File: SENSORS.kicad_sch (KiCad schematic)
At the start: 20 parts, among them U14 ICM-42688-P, U15 ICM-42688-P, U16 DPS368XTSA1, U17 IST8310

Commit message: Remove unused file
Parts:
- removed C47, C50: 100n, Capacitor_SMD:C_0402_1005Metric, symbol Device:C_Small
- removed R25, R26: 4.7K, Resistor_SMD:R_0402_1005Metric, symbol Device:R_Small
- removed R29: 100K, Resistor_SMD:R_0402_1005Metric, symbol Device:R_Small
- removed U17: IST8310, EasyEDA:LGA-16_L3.0-W3.0-P0.50-BL_SQ, symbol EasyEDA:HMC5883L-TR
- added C68: 100n, Capacitor_SMD:C_0402_1005Metric, symbol Device:C_Small
- added J10, J15: Conn_01x04, symbol Connector_Generic:Conn_01x04
- added R52, R53, R54, R55: 4.7K, Resistor_SMD:R_0402_1005Metric, symbol Device:R_Small
- added U2: BMP581, QFN10_BMP581_BOS, symbol BMP581:BMP581
- C51: value 4.7u -> 100n; LCSC C23733 -> C1525; LCSC Part C23733 -> C1525; MPN CL05A475MP5NRNC -> GRM022R60J104KE15D; Manufacturer Samsung Electro-Mechanics -> Murata Electronics
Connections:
- net +3V3_MCU: now also C49.1, U16.2 (CSB), U16.6 (VDDIO), C68.1, R52.1, R53.1, R54.1, R55.1, U2.1 (VDDIO), U2.6 (CSB)
- net +3V3_SENS: now also C51.1, U2.10 (VDD); no longer C49.1, U16.2 (CSB), U16.6 (VDDIO)
- net GND: now also C68.2, J10.2 (Pin_2), J15.2 (Pin_2), U2.3 (VSS), U2.5 (SDO), U2.8 (VSS), U2.9 (VSS)
- net I2C2.SCL: now also J15.4 (Pin_4), R54.2
- net I2C2.SDA: now also J15.3 (Pin_3), R55.2
- new net +5V_SYS: J10.1 (Pin_1), J15.1 (Pin_1)
- new net I2C1.SCL: J10.4 (Pin_4), R52.2, U2.2 (SCK)
- new net I2C1.SDA: J10.3 (Pin_3), R53.2, U2.4 (SDI)
- no-connect marks 9 -> 1
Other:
- note added: "I2C_1"
- note added: "I2C_2"
- note added: "shared with DPS368 sur I2C2 BMP581 sur I2C1"
- moved on the sheet: C48, U16

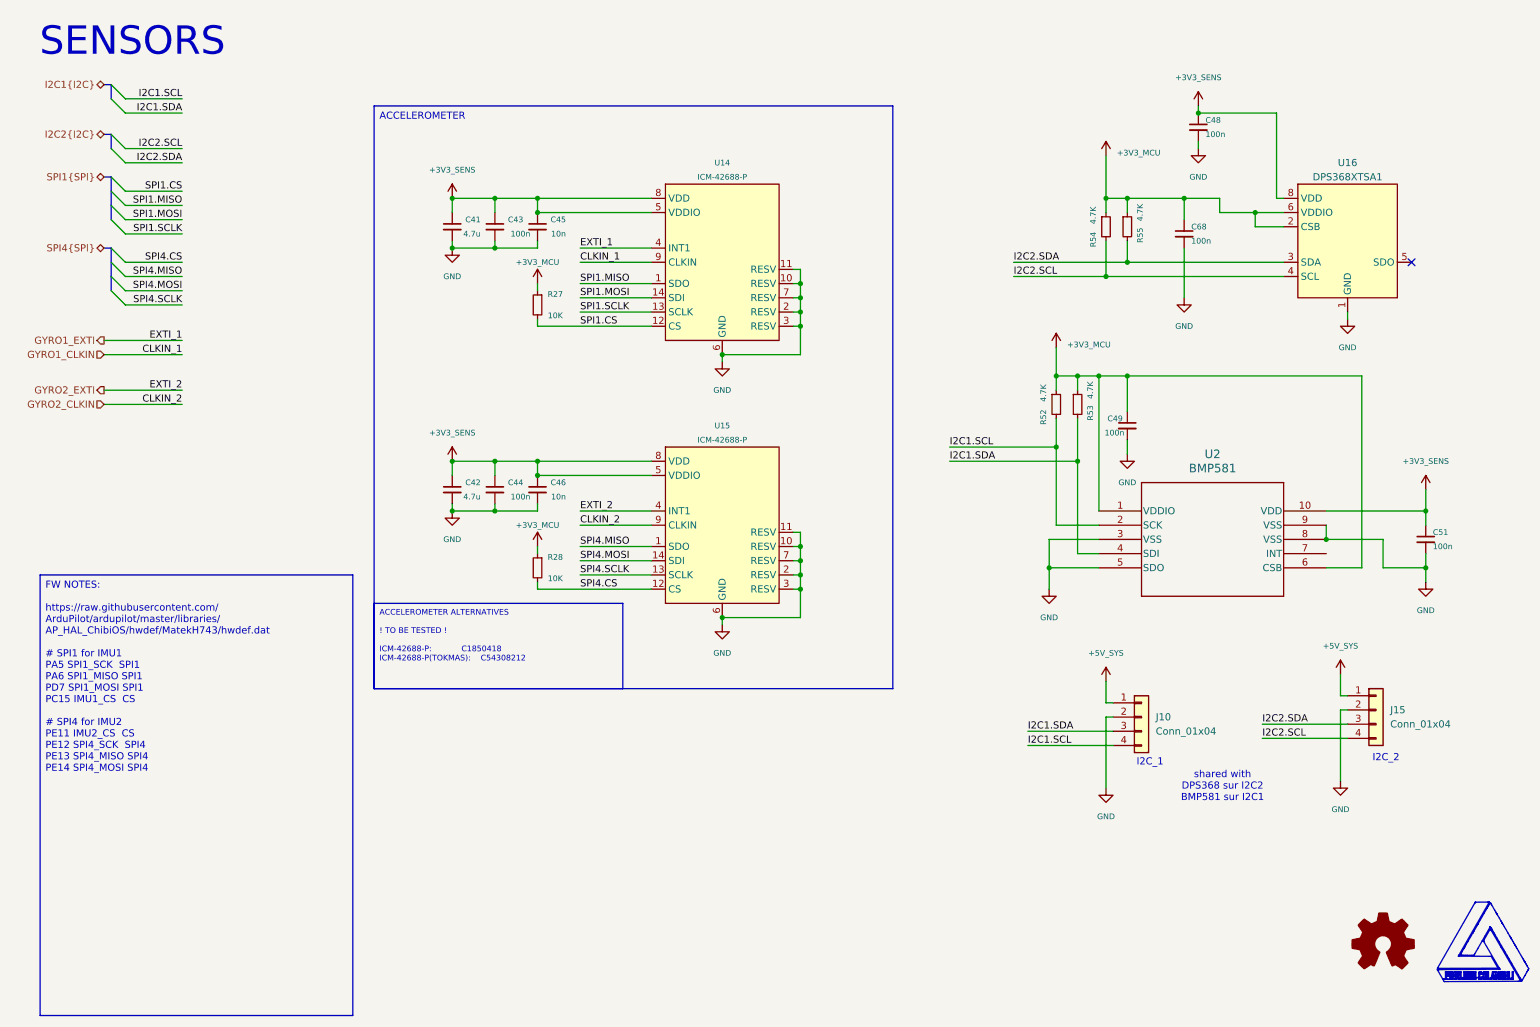
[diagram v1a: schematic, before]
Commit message: rework and work on IMUs
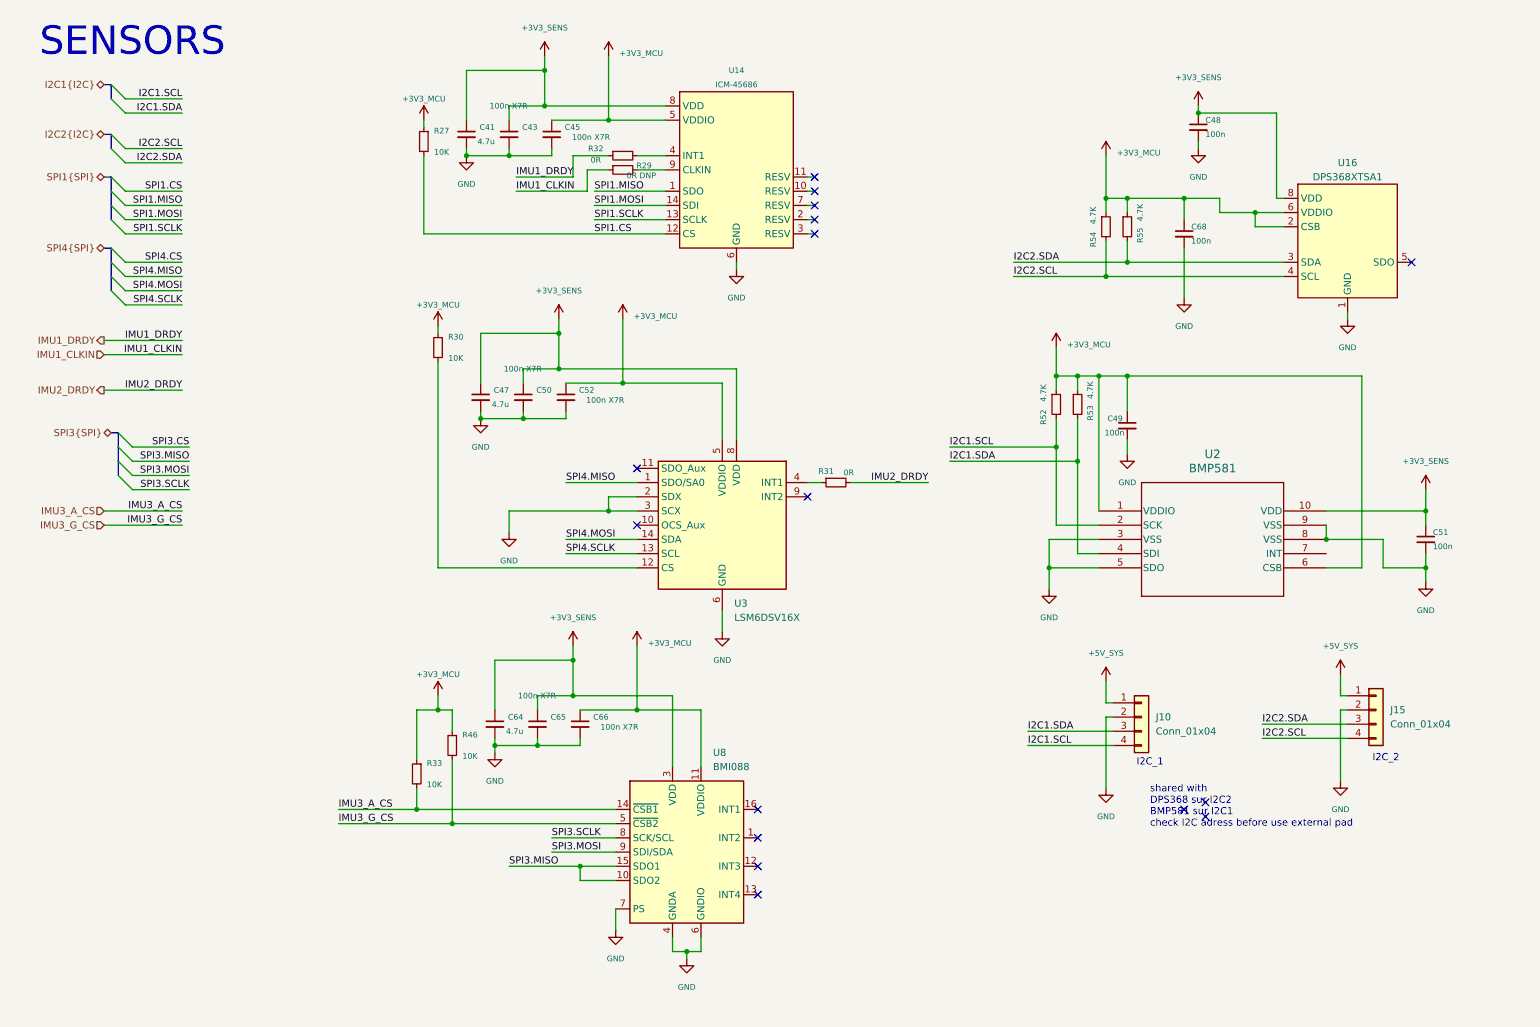
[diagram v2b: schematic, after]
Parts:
- removed C42: 4.7u, Capacitor_SMD:C_0402_1005Metric, symbol Device:C_Small
- removed C44: 100n, Capacitor_SMD:C_0402_1005Metric, symbol Device:C_Small
- removed C46: 10n, Capacitor_SMD:C_0402_1005Metric, symbol Device:C_Small
- removed R28: 10K, Resistor_SMD:R_0402_1005Metric, symbol Device:R_Small
- removed U15: ICM-42688-P, EasyEDA:LGA-14_L3.0-W2.5-P0.50-TL, symbol EasyEDA:ICM-42688-P
- added C47, C64: 4.7u, Capacitor_SMD:C_0402_1005Metric, symbol Device:C_Small
- added C50, C52, C65, C66: 100n X7R, Capacitor_SMD:C_0402_1005Metric, symbol Device:C_Small
- added R29: 0R DNP, Resistor_SMD:R_0402_1005Metric, symbol Device:R_Small
- added R30, R33, R46: 10K, Resistor_SMD:R_0402_1005Metric, symbol Device:R_Small
- added R31, R32: 0R, Resistor_SMD:R_0402_1005Metric, symbol Device:R_Small
- added U3: LSM6DSV16X, Package_LGA:LGA-14_3x2.5mm_P0.5mm_LayoutBorder3x4y, symbol Sensor_Motion:LSM6DSM
- added U8: BMI088, Package_LGA:Bosch_LGA-16_4.5x3mm_P0.5mm_LayoutBorder7x1y_ClockwisePinNumbering, symbol Sensor_Motion:BMI088
- C43: value 100n -> 100n X7R
- C45: value 10n -> 100n X7R
- U14: value ICM-42688-P -> ICM-45686
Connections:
- net +3V3_MCU: now also C45.1, U14.5 (VDDIO), C52.1, C66.1, R30.1, R33.1, R46.1, U3.5 (VDDIO), U8.11 (VDDIO)
- net +3V3_SENS: now also C47.1, C50.1, C64.1, C65.1, U3.8 (VDD), U8.3 (VDD); no longer C45.1, U14.5 (VDDIO)
- net GND: now also C47.2, C50.2, C52.2, C64.2, C65.2, C66.2, U3.2 (SDX), U3.3 (SCX), U3.6 (GND), U3.7 (GND), U8.2 (GNDA), U8.4 (GNDA), U8.6 (GNDIO), U8.7 (PS); no longer U14.10 (RESV), U14.11 (RESV), U14.2 (RESV), U14.3 (RESV), U14.7 (RESV)
- net SPI4.MISO: now also U3.1 (SDO/SA0)
- net SPI4.MOSI: now also U3.14 (SDA)
- net SPI4.SCLK: now also U3.13 (SCL)
- net GYRO1_CLKIN: no longer names the net of U14.9 (CLKIN)
- net GYRO1_CLKIN: now also R29.2
- net GYRO1_EXTI: no longer names the net of U14.4 (INT1)
- net GYRO1_EXTI: now also R32.2
- new net: R30.2, U3.12 (CS)
- new net: R31.1, U3.4 (INT1)
- new net IMU1_CLKIN: R29.1
- new net IMU1_DRDY: R32.1
- new net IMU2_DRDY: R31.2
- new net IMU3_A_CS: R33.2, U8.14 (~{CSB1})
- new net IMU3_G_CS: R46.2, U8.5 (~{CSB2})
- new net SPI3.MISO: U8.10 (SDO2), U8.15 (SDO1)
- new net SPI3.MOSI: U8.9 (SDI/SDA)
- new net SPI3.SCLK: U8.8 (SCK/SCL)
- no-connect marks 1 -> 16
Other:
- note added: "shared with DPS368 sur I2C2 BMP581 sur I2C1 check I2C adress before use external pad"
- note removed: "shared with DPS368 sur I2C2 BMP581 sur I2C1"
- moved on the sheet: C41, C43, C45, R27, U14

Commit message: update name
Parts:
- removed R27, R30, R33, R46: 10K, Resistor_SMD:R_0402_1005Metric, symbol Device:R_Small
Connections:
- net SPI4.CS: now also U3.12 (CS)
- no-connect marks 16 -> 13
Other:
- note removed: "SENSORS"
- company: Pierluigi Colangeli, PhD -> (none)
- title: LEVIA H7 -> (none)

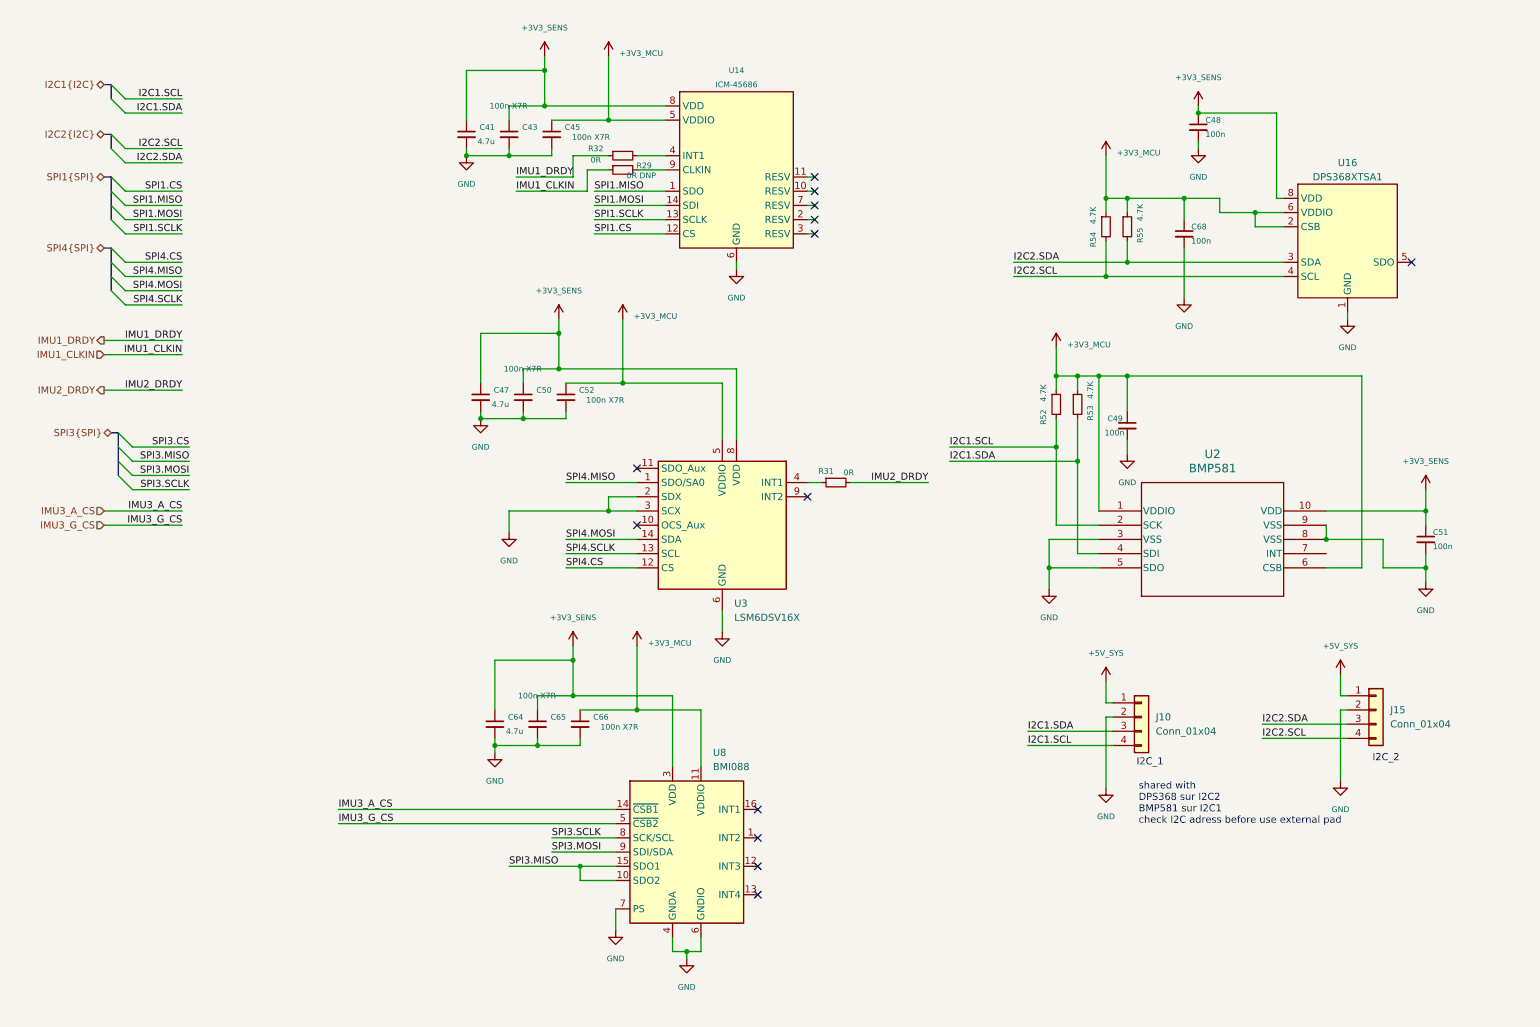
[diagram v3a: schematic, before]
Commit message: upsadte SPI4 set to Baro
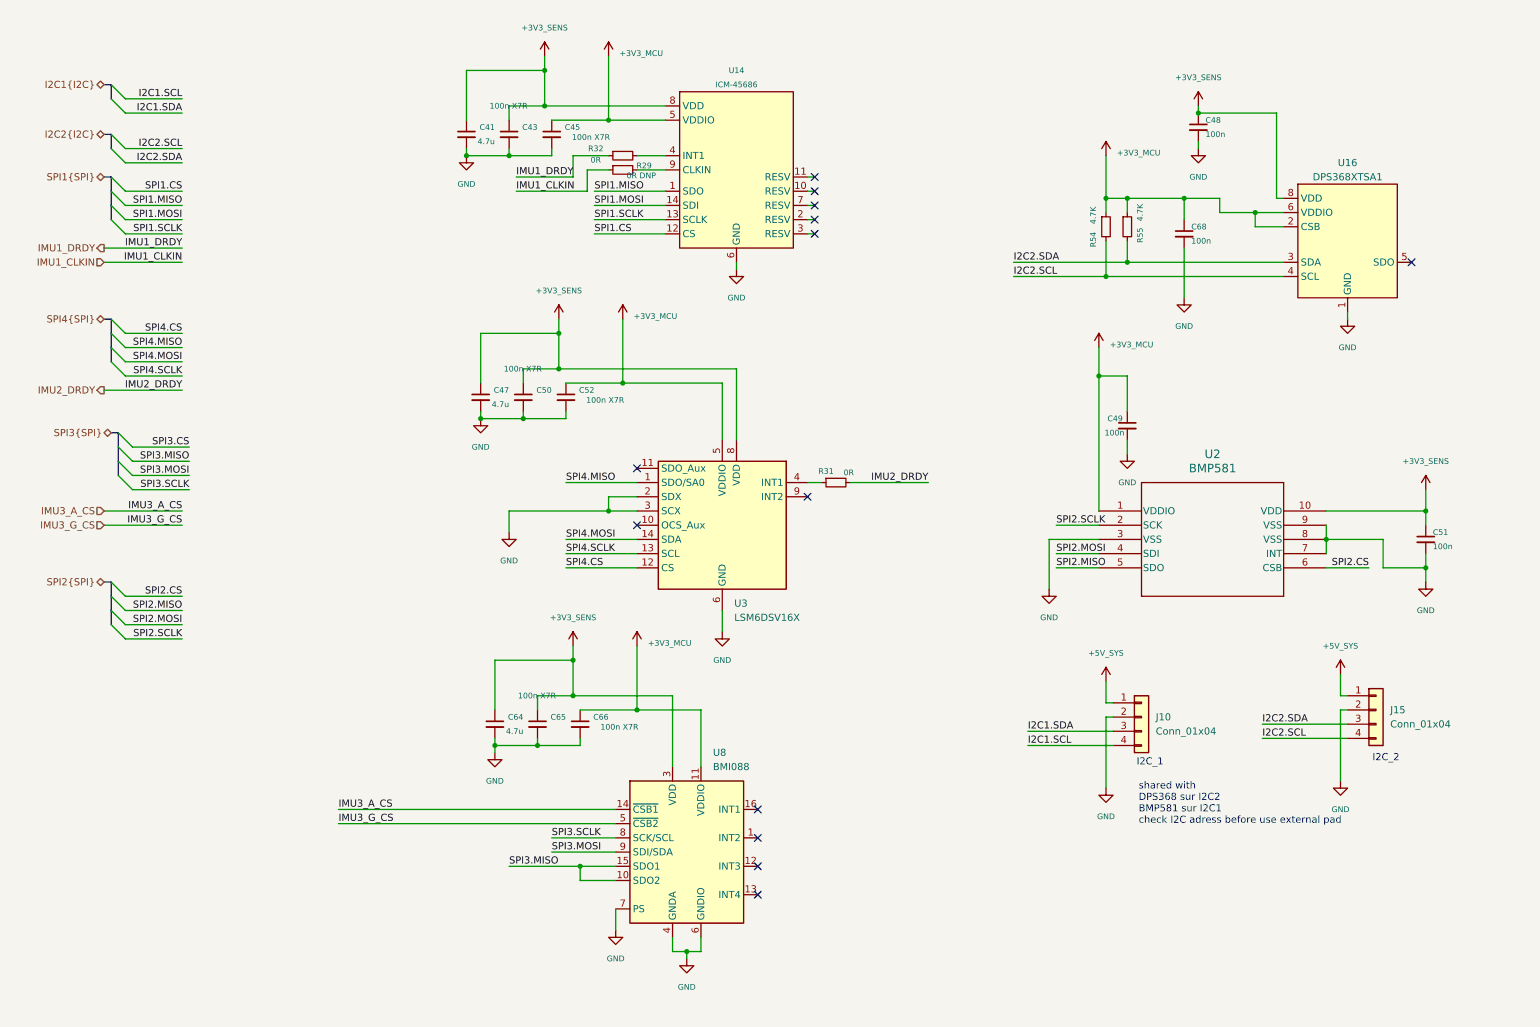
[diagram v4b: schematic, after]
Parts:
- removed R52, R53: 4.7K, Resistor_SMD:R_0402_1005Metric, symbol Device:R_Small
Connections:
- net +3V3_MCU: no longer U2.6 (CSB)
- net GND: now also U2.7 (INT); no longer U2.5 (SDO)
- net I2C1.SCL: no longer U2.2 (SCK)
- net I2C1.SDA: no longer U2.4 (SDI)
- new net SPI2.CS: U2.6 (CSB)
- new net SPI2.MISO: U2.5 (SDO)
- new net SPI2.MOSI: U2.4 (SDI)
- new net SPI2.SCLK: U2.2 (SCK)
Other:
- title: (none) -> H743_ARDUPILOT

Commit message: update 1
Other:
- note removed: "shared with DPS368 sur I2C2 BMP581 sur I2C1 check I2C adress before use external pad"
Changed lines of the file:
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@@
-		)
-	)
-	(text "shared with \nDPS368 sur I2C2\nBMP581 sur I2C1\ncheck I2C adress before use external pad"
-		(exclude_from_sim no)
-		(at 212.852 155.194 0)
-		(effects
-			(font
-				(size 1.27 1.27)
-			)
-			(justify left)
 		)
 	)

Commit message: re annotate componant globaly
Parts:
- R29: value 0R DNP -> 0R
- U7: renamed from U14; LCSC C1850418 -> C22459454; LCSC Part C1850418 -> C22459454; MPN ICM-42688-P -> ICM-45686
- renumbered C41 to C27, C47 to C28, C64 to C29, C43 to C30, C50 to C31, C65 to C32, C45 to C33, C52 to C34, C66 to C35, C49 to C36, C68 to C37, C48 to C38, C51 to C39, J10 to J8, J15 to J9, R32 to R28, R31 to R30, R54 to R31, R55 to R32, U8 to U5, U3 to U6, U2 to U8, U16 to U9

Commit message: fix sensor symbols for ICM-45686 and LSM6DSV16X
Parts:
- U6: symbol Sensor_Motion:LSM6DSM -> H743_Ardupilot:LSM6DSV16X
- U7: symbol EasyEDA:ICM-42688-P -> H743_Ardupilot:ICM-45686
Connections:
- net +3V3_MCU: no longer U7.5 (VDDIO)
- net +3V3_SENS: no longer U7.8 (VDD)
- net GND: no longer U7.6 (GND)
- net SPI1.CS: no longer U7.12 (CS)
- net SPI1.MISO: no longer U7.1 (SDO)
- net SPI1.MOSI: no longer U7.14 (SDI)
- net SPI1.SCLK: no longer U7.13 (SCLK)
- net at R28.2: no longer U7.4 (INT1)
- net at R29.2: no longer U7.9 (CLKIN)
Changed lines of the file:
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@@
 	)
 	(symbol
-		(lib_id "Sensor_Motion:LSM6DSM")
+		(lib_id "H743_Ardupilot:LSM6DSV16X")
 		(at 138.43 105.41 0)
 		(unit 1)
@@
 	)
 	(symbol
-		(lib_name "ICM-42688-P_1")
-		(lib_id "EasyEDA:ICM-42688-P")
+		(lib_name "ICM-45686")
+		(lib_id "H743_Ardupilot:ICM-45686")
 		(at 140.97 41.91 0)
 		(unit 1)
